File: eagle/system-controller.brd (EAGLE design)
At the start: 99 x 100 mm, 233 parts, among them CN1 22u, IC2 TS4100, J1 1, Q0 MOSFET-P-N-PAIR, Q1 MOSFET-P-N-PAIR, Q10 DNP/NTR4101P, Q12 DNP/NTR4101P, Q13 DON3035L, Q2 MOSFET-P-N-PAIR, Q3 MOSFET-P-N-PAIR, Q4 MOSFET-P-N-PAIR, Q5 MOSFET-P-N-PAIR, Q6 MOSFET-P-N-PAIR, Q7 MOSFET-P-N-PAIR, SW0 TPS25944LRVCRWQFN-20-3X4, SW1 TPS25944LRVCRWQFN-20-3X4, SW2 TPS25944LRVCRWQFN-20-3X4, SW3 TPS25944LRVCRWQFN-20-3X4, SW4 TPS25944LRVCRWQFN-20-3X4, SW5 TPS25944LRVCRWQFN-20-3X4, SW6 TPS25944LRVCRWQFN-20-3X4, SW7 TPS25944LRVCRWQFN-20-3X4, U1 MEGA128-A, X1 8 MHz CRYSTAL-ABRACON-ABM3-SMD

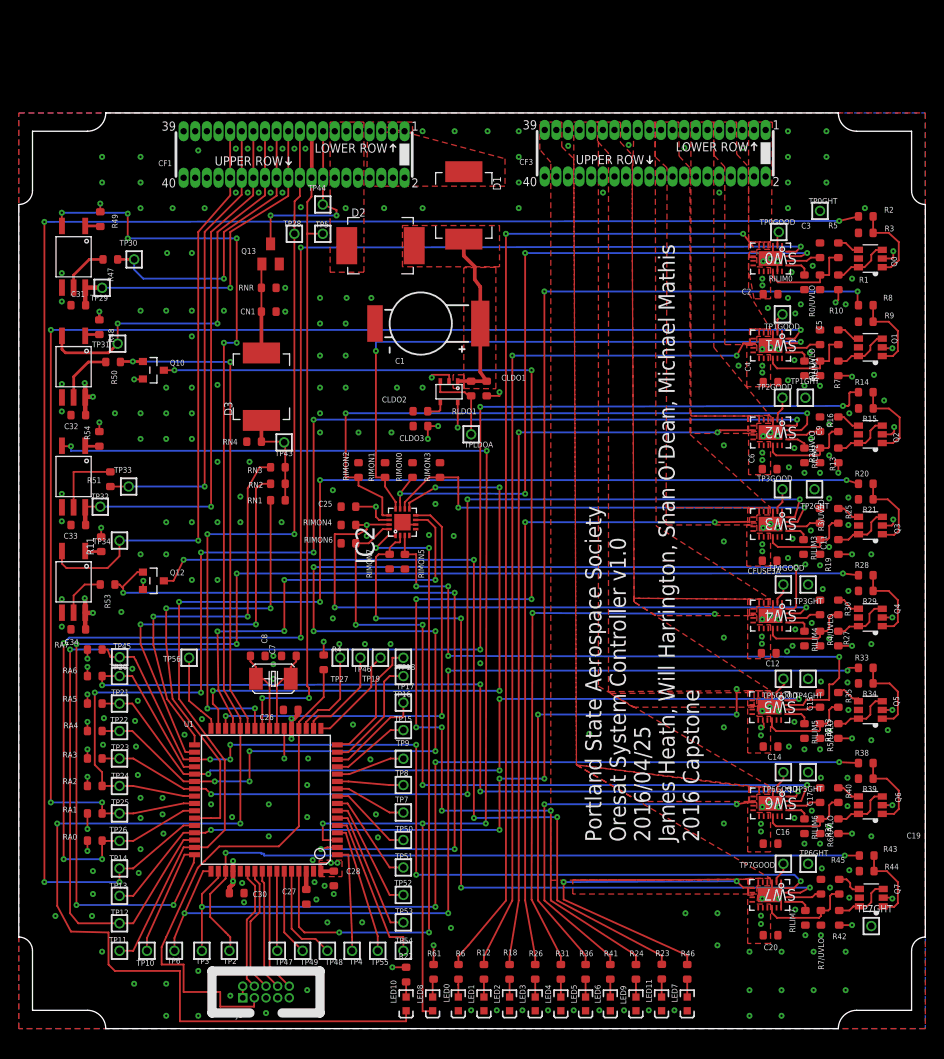
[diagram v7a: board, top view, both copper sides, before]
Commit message: Added names to missing parts and updated the BOM and Parts Selection doc accordingly
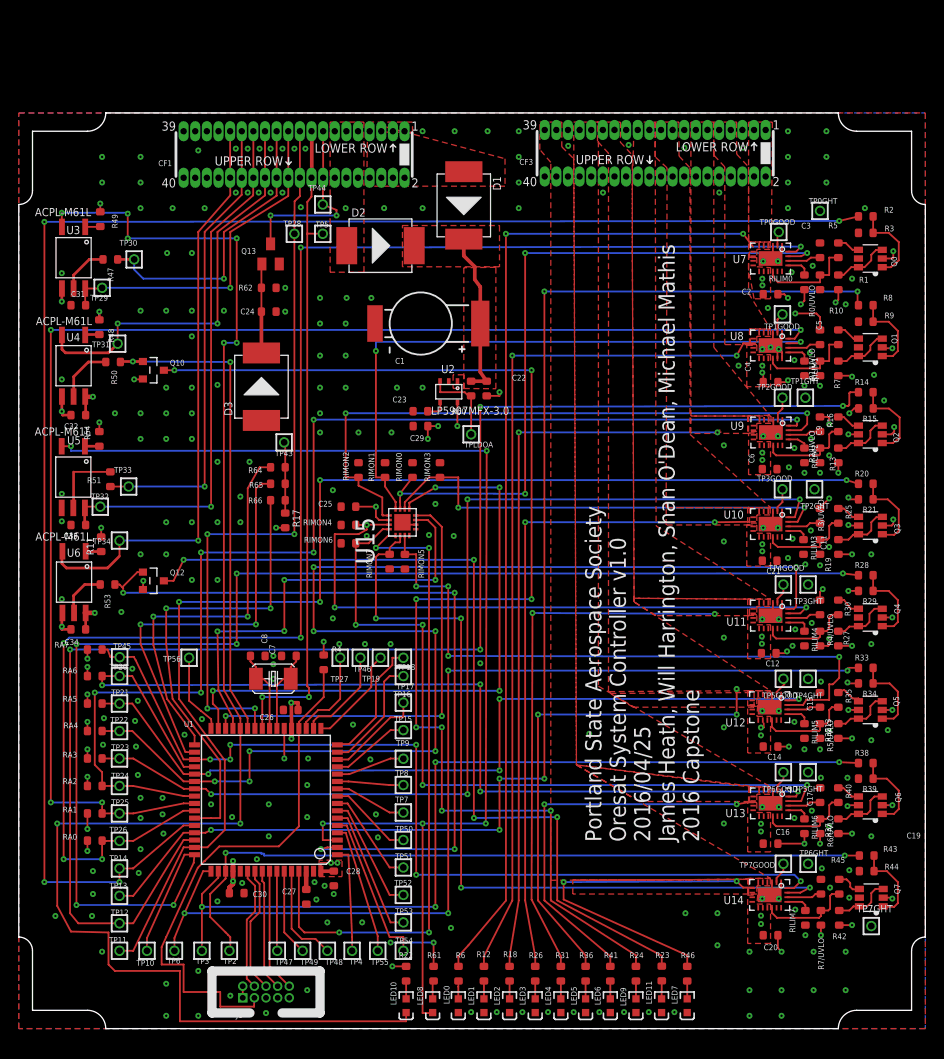
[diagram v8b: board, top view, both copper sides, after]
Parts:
- removed IC2: TS4100, system-controller:QFN50P400X400X80-17N
- removed RN4: 390, rcl_custom:.0603-B-NOSILK
- removed SW2: TPS25944LRVCRWQFN-20-3X4, system-controller:QFN-20-L
- removed U$1, U$2, U$3, U$4: ACPL-M61L, psas_c3_team05:ACPL-M61L
- removed U$8: AAT3215, psas_c3_team05:AAT3215
- added R17: 390, rcl_custom:.0603-B-NOSILK
- added U15: TS4100, system-controller:QFN50P400X400X80-17N
- added U2: LP5907MFX-3.0, system-controller:SOT-23
- added U3, U4, U5, U6: ACPL-M61L, system-controller:ACPL-M61L
- added U9: TPS25944LRVCRWQFN-20-3X4, system-controller:QFN-20-L
- moved LED0 0.20 mm to (48.0, 2.50)
- moved LED1 0.20 mm to (50.8, 2.50)
- moved LED10 0.20 mm to (42.3, 2.50)
- moved LED11 0.20 mm to (70.2, 2.50)
- moved LED2 0.20 mm to (53.6, 2.50)
- moved LED3 0.20 mm to (56.4, 2.50)
- moved LED4 0.20 mm to (59.2, 2.50)
- moved LED5 0.20 mm to (61.9, 2.50)
- moved LED6 0.20 mm to (64.6, 2.50)
- moved LED7 0.20 mm to (73.0, 2.50)
- moved LED8 0.20 mm to (45.2, 2.50)
- moved LED9 0.20 mm to (67.4, 2.50)
- moved R12 0.20 mm to (50.8, 6.00)
- moved R18 0.20 mm to (53.6, 6.00)
- moved R23 0.20 mm to (70.2, 6.02)
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- renumbered CFUSE3A to C21, CLDO1 to C22, CLDO2 to C23, CLDO3 to C29, CN1 to C24, RLDO1 to R60, RN1 to R66, RN2 to R65, RN3 to R64, RNR to R62, SW0 to U7, SW1 to U8, SW3 to U10, SW4 to U11, SW5 to U12, SW6 to U13, SW7 to U14
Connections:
- net 3V: now also U15.14, U2.5, U4.5, U6.5; no longer IC2.14, U$2.5, U$4.5, U$8.5
- net GND: now also R17.2, U15.17, U15.4, U15.6, U2.2, U3.3, U4.3, U5.3, U6.3, U9.1, U9.15, U9.16, U9.21, U9.3; no longer IC2.17, IC2.4, IC2.6, RN4.2, SW2.1, SW2.15, SW2.16, SW2.21, SW2.3, U$1.3, U$2.3, U$3.3, U$4.3, U$8.2
- net N$10: now also U9.14; no longer SW2.14
- net N$107: now also U15.1; no longer IC2.1
- net N$109: now also R17.1; no longer RN4.1
- net N$16: now also U5.4; no longer U$3.4
- net N$18: now also U6.4; no longer U$4.4
- net N$19: now also U9.17; no longer SW2.17
- net N$22: now also U2.3; no longer U$8.3
- net N$23: now also U2.4; no longer U$8.4
- net N$24: now also U4.4; no longer U$2.4
- net N$4: now also U5.1; no longer U$3.1
- net N$46: now also U15.7; no longer IC2.7
- net N$47: now also U15.8; no longer IC2.8
- net N$48: now also U15.9; no longer IC2.9
- net N$5: now also U3.4; no longer U$1.4
- net N$54: now also U6.1; no longer U$4.1
- net N$58: now also U3.1; no longer U$1.1
- net N$59: now also U9.2; no longer SW2.2
- net N$62: now also U9.18; no longer SW2.18
- net N$8: now also U4.1; no longer U$2.1
- net TXD0: now also U5.2; no longer U$3.2
- net TXD1: now also U3.2; no longer U$1.2
- net UART_FC_TX: now also U4.2; no longer U$2.2
- net UART_FC_VCC: now also U3.5; no longer U$1.5
- net UART_LGR_TX: now also U6.2; no longer U$4.2
- net UART_LGR_VCC: now also U5.5; no longer U$3.5
- net V+: now also U2.1; no longer U$8.1
- net VBUS: now also U9.10, U9.11, U9.12, U9.13, U9.9; no longer SW2.10, SW2.11, SW2.12, SW2.13, SW2.9
- net VCB0_IMON: now also U15.11; no longer IC2.11
- net VCB1_IMON: now also U15.12; no longer IC2.12
- net VCB2: now also U9.4, U9.5, U9.6, U9.7, U9.8; no longer SW2.4, SW2.5, SW2.6, SW2.7, SW2.8
- net VCB2_!FLT: now also U9.20; no longer SW2.20
- net VCB2_IMON: now also U15.13, U9.19; no longer IC2.13, SW2.19
- net VCB3_IMON: now also U15.10; no longer IC2.10
- net VCB4_IMON: now also U15.15; no longer IC2.15
- net VCB5_IMON: now also U15.3; no longer IC2.3
- net VCB6_IMON: now also U15.16; no longer IC2.16
- net VCB7_IMON: now also U15.2; no longer IC2.2
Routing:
- net GND: track 39.6 -> 78.4 mm, vias 285 -> 278
- net 3V: track 51.5 -> 55.9 mm, vias 31 -> 30
- net VCB2: track 84.2 -> 80.8 mm
- net N$109: track 11.3 -> 7.92 mm
- net V+: track 20.7 -> 19.1 mm
- net VBUS: track 24.1 -> 25.2 mm
